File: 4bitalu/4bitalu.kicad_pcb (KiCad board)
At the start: 2 copper layers, 87.6 x 81.3 mm, 34 parts, among them J1 Power, SW1 Opcode, SW2 Input Value, U1 74LS153 - 0, U2 74LS153 - 1, U3 74LS175, U4 74LS283, U5 74LS00 Stage0-1, U6 74LS00 Stage0-2, U7 74LS00 - Stage1

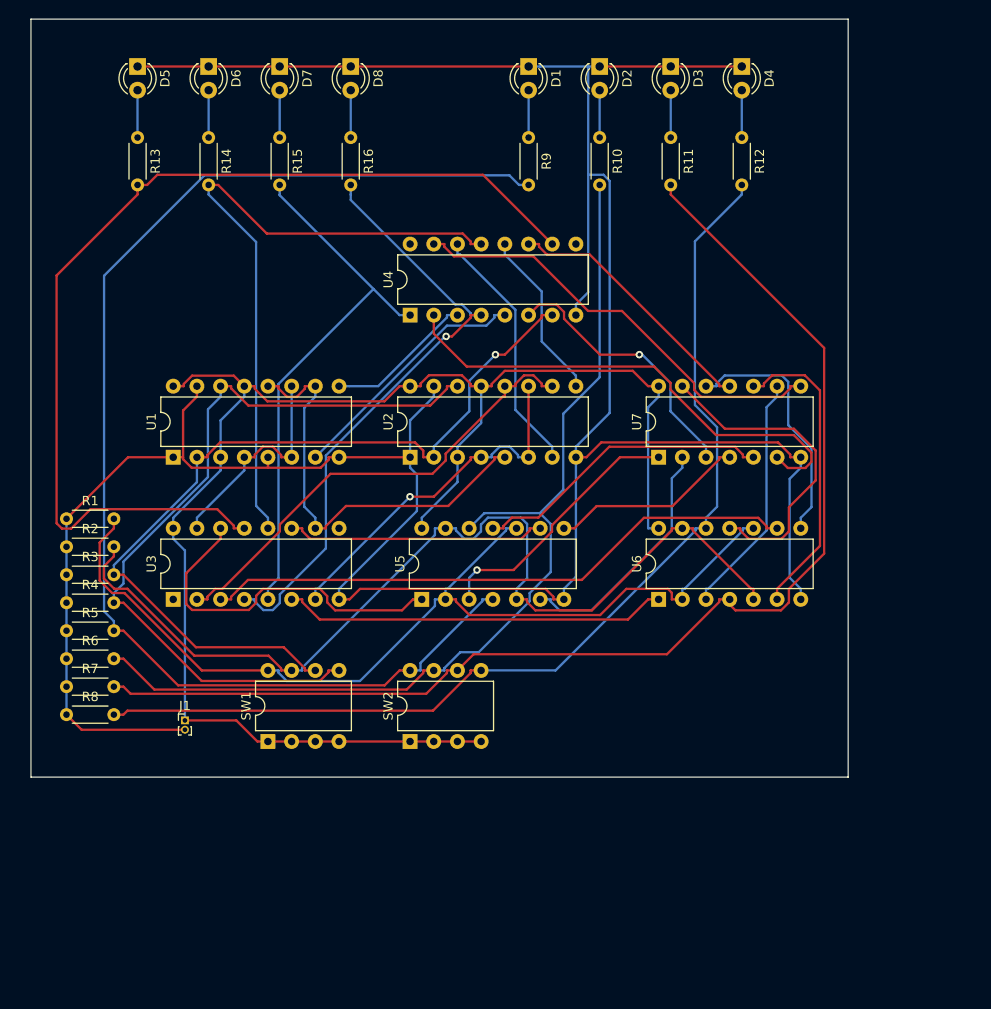
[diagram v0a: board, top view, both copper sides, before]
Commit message: Rev 2 of PCB design
Known issues:

 * Pulldown resistors are too high (should be 1k)
 * Missing capacitors for power inputs on chips
 * Inputs on unused NAND gates are not tied high
 * Clock switch is in unexepected orientation
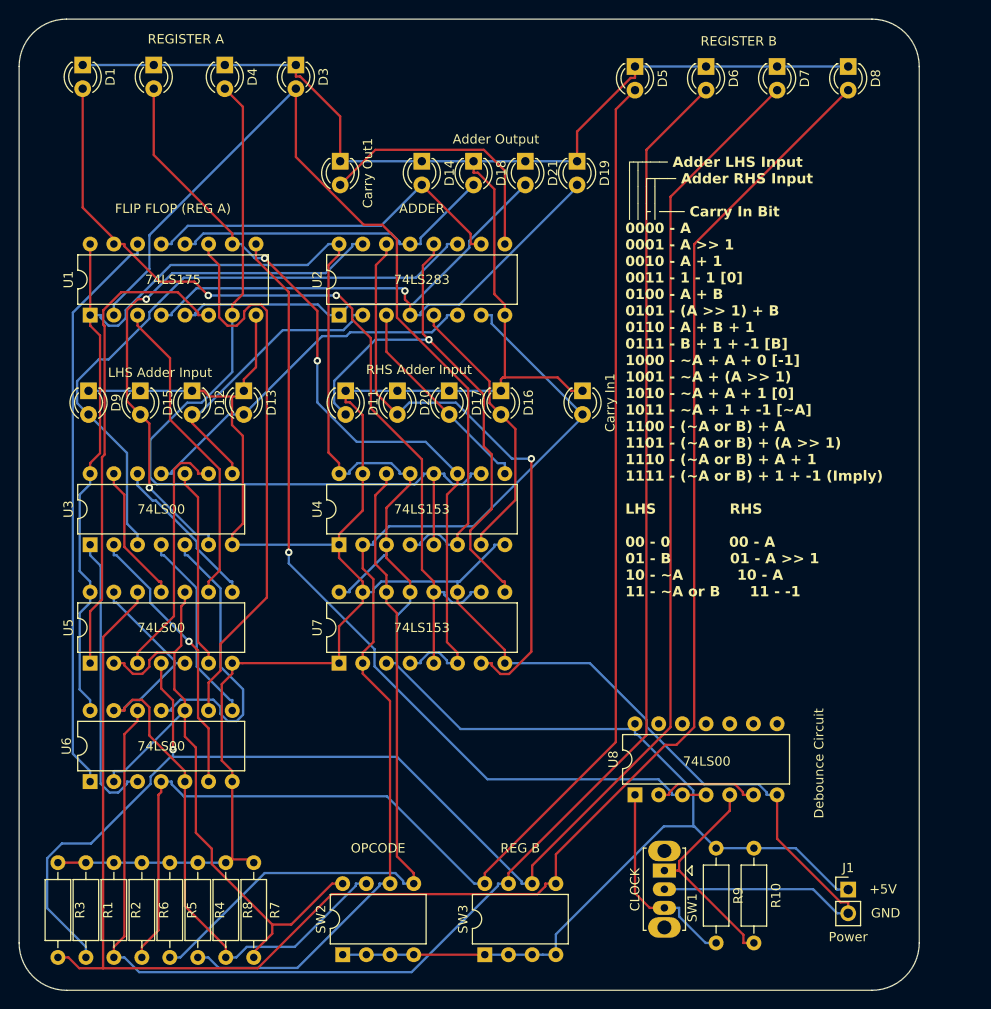
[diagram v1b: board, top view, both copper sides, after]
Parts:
- removed R11, R12, R13, R14, R15, R16: 1.5k, Resistor_THT:R_Axial_DIN0204_L3.6mm_D1.6mm_P5.08mm_Horizontal
- added Carry In1: CarryIn, LED_THT:LED_D3.0mm, F.Cu at (88.4, 93.2)
- added Carry Out1: CarryOut, LED_THT:LED_D3.0mm, F.Cu at (62.4, 68.6)
- added D1: RegBit3, LED_THT:LED_D3.0mm, F.Cu at (34.8, 58.3)
- added D11: RHS3, LED_THT:LED_D3.0mm, F.Cu at (63.0, 93.2)
- added D12: LHS1, LED_THT:LED_D3.0mm, F.Cu at (46.5, 93.2)
- added D13: LHS0, LED_THT:LED_D3.0mm, F.Cu at (52.0, 93.2)
- added D15: LHS2, LED_THT:LED_D3.0mm, F.Cu at (40.9, 93.2)
- added D16: RHS0, LED_THT:LED_D3.0mm, F.Cu at (79.6, 93.2)
- added D17: RHS1, LED_THT:LED_D3.0mm, F.Cu at (74.1, 93.2)
- added D2: RegBit2, LED_THT:LED_D3.0mm, F.Cu at (42.4, 58.3)
- added D20: RHS2, LED_THT:LED_D3.0mm, F.Cu at (68.5, 93.2)
- added D3: RegBit0, LED_THT:LED_D3.0mm, F.Cu at (57.6, 58.3)
- added D4: RegBit1, LED_THT:LED_D3.0mm, F.Cu at (50.0, 58.3)
- added D9: LHS3, LED_THT:LED_D3.0mm, F.Cu at (35.4, 93.2)
- added SW1: SW_SPDT, Button_Switch_THT:SW_Slide_1P2T_CK_OS102011MS2Q, F.Cu at (97.1, 144.6)
- added U8: 74LS00, Package_DIP:DIP-14_W7.62mm, F.Cu at (94.0, 136.5)
- D14: renamed from D5; value RegBit3 -> MidBit3
- D18: renamed from D6; value RegBit2 -> MidBit2
- D19: renamed from D8; value RegBit0 -> MidBit0
- D21: renamed from D7; value RegBit1 -> MidBit1
- J1: footprint Connector_PinHeader_1.00mm:PinHeader_1x02_P1.00mm_Vertical -> Connector_PinHeader_2.54mm:PinHeader_1x02_P2.54mm_Vertical
- R1: renamed from R7; footprint Resistor_THT:R_Axial_DIN0204_L3.6mm_D1.6mm_P5.08mm_Horizontal -> Resistor_THT:R_Axial_DIN0207_L6.3mm_D2.5mm_P10.16mm_Horizontal
- R10, R9: value 1.5k -> 25k; footprint Resistor_THT:R_Axial_DIN0204_L3.6mm_D1.6mm_P5.08mm_Horizontal -> Resistor_THT:R_Axial_DIN0207_L6.3mm_D2.5mm_P10.16mm_Horizontal
- R2: renamed from R6; footprint Resistor_THT:R_Axial_DIN0204_L3.6mm_D1.6mm_P5.08mm_Horizontal -> Resistor_THT:R_Axial_DIN0207_L6.3mm_D2.5mm_P10.16mm_Horizontal
- R3: renamed from R8; footprint Resistor_THT:R_Axial_DIN0204_L3.6mm_D1.6mm_P5.08mm_Horizontal -> Resistor_THT:R_Axial_DIN0207_L6.3mm_D2.5mm_P10.16mm_Horizontal
- R4: renamed from R3; footprint Resistor_THT:R_Axial_DIN0204_L3.6mm_D1.6mm_P5.08mm_Horizontal -> Resistor_THT:R_Axial_DIN0207_L6.3mm_D2.5mm_P10.16mm_Horizontal
- R5: renamed from R4; footprint Resistor_THT:R_Axial_DIN0204_L3.6mm_D1.6mm_P5.08mm_Horizontal -> Resistor_THT:R_Axial_DIN0207_L6.3mm_D2.5mm_P10.16mm_Horizontal
- R6: renamed from R5; footprint Resistor_THT:R_Axial_DIN0204_L3.6mm_D1.6mm_P5.08mm_Horizontal -> Resistor_THT:R_Axial_DIN0207_L6.3mm_D2.5mm_P10.16mm_Horizontal
- R7: renamed from R1; footprint Resistor_THT:R_Axial_DIN0204_L3.6mm_D1.6mm_P5.08mm_Horizontal -> Resistor_THT:R_Axial_DIN0207_L6.3mm_D2.5mm_P10.16mm_Horizontal
- R8: renamed from R2; footprint Resistor_THT:R_Axial_DIN0204_L3.6mm_D1.6mm_P5.08mm_Horizontal -> Resistor_THT:R_Axial_DIN0207_L6.3mm_D2.5mm_P10.16mm_Horizontal
- moved R9 78.8 mm to (102.7, 142.2)
- moved R10 78.0 mm to (106.7, 142.2)
- moved J1 73.4 mm to (116.8, 146.7)
- moved U3 61.7 mm to (35.6, 109.7)
- moved U5 61.3 mm to (35.6, 122.4)
- moved R7 42.0 mm to (53.1, 143.8), turned to -90 degrees
- moved U6 40.6 mm to (35.6, 135.1)
- moved R8 37.9 mm to (50.1, 143.8), turned to -90 degrees
- moved R4 33.9 mm to (47.1, 143.8), turned to -90 degrees
- moved D14 32.1 mm to (71.1, 68.6)
- moved U1 31.8 mm to (35.6, 85.1)
- moved D18 30.2 mm to (76.7, 68.6)
- moved R5 30.0 mm to (44.1, 143.8), turned to -90 degrees
- moved D21 28.2 mm to (82.2, 68.6)
- moved D19 26.3 mm to (87.8, 68.6)
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- renumbered D1 to D5, D2 to D6, D3 to D7, D4 to D8, SW1 to SW2, SW2 to SW3, U3 to U1, U4 to U2, U7 to U3, U1 to U4, U6 to U5, U5 to U6, U2 to U7
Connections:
- D14 pad 2: Net-(D5-A) -> Net-(D14-A)
- D18 pad 2: Net-(D6-A) -> Net-(D18-A)
- D19 pad 2: Net-(D8-A) -> Net-(D19-A)
- D21 pad 2: Net-(D7-A) -> Net-(D21-A)
- D5 pad 2: Net-(D1-A) -> Net-(D5-A)
- D6 pad 2: Net-(D2-A) -> Net-(D6-A)
- D7 pad 2: Net-(D3-A) -> Net-(D7-A)
- D8 pad 2: Net-(D4-A) -> Net-(D8-A)
- R1 pad 2: Net-(R11-Pad2) -> Net-(D7-A)
- R10 pad 1: Net-(D2-A) -> +5V
- R10 pad 2: Net-(R10-Pad2) -> Net-(SW1-A)
- R2 pad 2: Net-(R10-Pad2) -> Net-(D6-A)
- R3 pad 2: Net-(R12-Pad2) -> Net-(D8-A)
- R6 pad 2: Net-(R5-Pad2) -> Net-(D5-A)
- R9 pad 1: Net-(D1-A) -> +5V
- R9 pad 2: Net-(R5-Pad2) -> Net-(SW1-C)
- SW3 pad 5: Net-(R12-Pad2) -> Net-(D8-A)
- SW3 pad 6: Net-(R11-Pad2) -> Net-(D7-A)
- SW3 pad 7: Net-(R10-Pad2) -> Net-(D6-A)
- SW3 pad 8: Net-(R5-Pad2) -> Net-(D5-A)
- U1 pad 1: unconnected-(U3-~{Mr}-Pad1) -> +5V
- U1 pad 10: Net-(U1-I0b) -> Net-(D2-A)
- U1 pad 12: Net-(U3-D2) -> Net-(D18-A)
- U1 pad 13: Net-(U3-D3) -> Net-(D14-A)
- U1 pad 15: Net-(U1-I0a) -> Net-(D1-A)
- U1 pad 2: Net-(U2-I0b) -> Net-(D3-A)
- U1 pad 4: Net-(U3-D0) -> Net-(D19-A)
- U1 pad 5: Net-(U3-D1) -> Net-(D21-A)
- U1 pad 7: Net-(U2-I0a) -> Net-(D4-A)
- U1 pad 9: unconnected-(U3-Cp-Pad9) -> Net-(U1-Cp)
- U2 pad 1: Net-(U3-D1) -> Net-(D21-A)
- U2 pad 10: Net-(U3-D3) -> Net-(D14-A)
- U2 pad 11: Net-(U4-B4) -> Net-(D9-A)
- U2 pad 13: Net-(U3-D2) -> Net-(D18-A)
- U2 pad 15: Net-(U4-B3) -> Net-(D15-A)
- U2 pad 16: unconnected-(U4-VCC-Pad16) -> +5V
- U2 pad 2: Net-(U4-B2) -> Net-(D12-A)
- U2 pad 4: Net-(U3-D0) -> Net-(D19-A)
- U2 pad 6: Net-(U4-B1) -> Net-(D13-A)
- U2 pad 9: unconnected-(U4-C4-Pad9) -> Net-(Carry Out1-A)
- U3 pad 11: Net-(U4-B4) -> Net-(D13-A)
- U3 pad 3: Net-(U4-B1) -> Net-(D9-A)
- U3 pad 6: Net-(U4-B2) -> Net-(D15-A)
- U3 pad 8: Net-(U4-B3) -> Net-(D12-A)
- U4 pad 10: Net-(U1-I0b) -> Net-(D4-A)
- U4 pad 11: Net-(U1-I0a) -> Net-(D2-A)
- U4 pad 12: Net-(U1-I0b) -> Net-(D4-A)
- U4 pad 4: Net-(U1-I0a) -> Net-(D3-A)
- U4 pad 5: GND -> Net-(D4-A)
- U4 pad 6: Net-(U1-I0a) -> Net-(D3-A)
- U5 pad 12: Net-(R12-Pad2) -> Net-(D8-A)
- U5 pad 4: Net-(R11-Pad2) -> Net-(D7-A)
- U6 pad 12: Net-(R10-Pad2) -> Net-(D6-A)
- U6 pad 4: Net-(R5-Pad2) -> Net-(D5-A)
- U7 pad 10: Net-(U2-I0b) -> Net-(D1-A)
- U7 pad 11: Net-(U2-I0a) -> GND
- U7 pad 12: Net-(U2-I0b) -> Net-(D1-A)
- U7 pad 4: Net-(U2-I0a) -> Net-(D2-A)
- U7 pad 5: Net-(U1-I0b) -> Net-(D1-A)
- U7 pad 6: Net-(U2-I0a) -> Net-(D2-A)
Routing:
- net Net-(D8-A): track 5.08 -> 198.4 mm
- net Net-(D7-A): track 5.08 -> 181.6 mm, vias 0 -> 1
- net Net-(D6-A): track 5.08 -> 168.4 mm
- net Net-(D5-A): track 5.08 -> 150.9 mm
- net Net-(R5-Pad2): track 136.4 -> 0.00 mm
- net Net-(R11-Pad2): track 131.8 -> 0.00 mm
- net Net-(R12-Pad2): track 112.4 -> 0.00 mm
- net Net-(U3-D3): track 110.1 -> 0.00 mm
- net Net-(R10-Pad2): track 107.2 -> 0.00 mm
- net +5V: track 164.3 -> 257.1 mm
- net Net-(U1-Cp): track 0.00 -> 91.9 mm, vias 0 -> 1
- net Net-(D3-A): track 5.08 -> 96.9 mm
- net Net-(D1-A): track 5.08 -> 94.8 mm, vias 0 -> 2
- net Net-(D4-A): track 5.08 -> 92.8 mm
- net Net-(D2-A): track 5.08 -> 88.0 mm, vias 0 -> 2
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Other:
- board size 87.6 x 81.3 mm -> 96.5 x 104.1 mm
- board text added: "+5V"
- board text added: "Adder Output"
- board text added: "Debounce Circuit"
- board text added: "GND"
- board text added: "LHS Adder Input"
- board text added: "REGISTER A"
- board text added: "REGISTER B"
- board text added: "RHS Adder Input"
- board text added: "┌┬─── Adder LHS Input ││┌┬── Adder RHS Input ││││ ││├│─── Carry In Bit 0000 - A 0001 - A >> 1 0010 - A + 1 0011 - 1 - 1 [0] 0100 - A + B 0101 - (A >> 1) + B 0110 - A + B + 1 0111 - B + 1 + -1 [B] 1000 - ~A + A + 0 [-1] 1001 - ~A + (A >> 1) 1010 - ~A + A + 1 [0] 1011 - ~A + 1 + -1 [~A] 1100 - (~A or B) + A 1101 - (~A or B) + (A >> 1) 1110 - (~A or B) + A + 1 1111 - (~A or B) + 1 + -1 (Imply) LHS R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"

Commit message: Revision 3 mostly ready
 * Adds caps on power
 * Inverts logic for clock switch
 * Adds optional clock LED
 * Changes pulldown resistors to 1k

Note: this design should also work with 3.3v logic and LEDs
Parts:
- added C1: .1uf, Capacitor_THT:C_Disc_D3.0mm_W1.6mm_P2.50mm, F.Cu at (32.0, 77.5)
- added C2: .1uf, Capacitor_THT:C_Disc_D3.0mm_W1.6mm_P2.50mm, F.Cu at (58.7, 77.5)
- added C3: .1uf, Capacitor_THT:C_Disc_D3.0mm_W1.6mm_P2.50mm, F.Cu at (31.9, 102.1)
- added C4: .1uf, Capacitor_THT:C_Disc_D3.0mm_W1.6mm_P2.50mm, F.Cu at (58.5, 102.0)
- added C5: .1uf, Capacitor_THT:C_Disc_D3.0mm_W1.6mm_P2.50mm, F.Cu at (31.8, 114.7)
- added C6: .1uf, Capacitor_THT:C_Disc_D3.0mm_W1.6mm_P2.50mm, F.Cu at (58.2, 114.8)
- added C7: .1uf, Capacitor_THT:C_Disc_D3.0mm_W1.6mm_P2.50mm, F.Cu at (31.7, 127.5)
- added C8: .1uf, Capacitor_THT:C_Disc_D3.0mm_W1.6mm_P2.50mm, F.Cu at (90.2, 128.9)
- added ClockState1: ClockState, LED_THT:LED_D3.0mm, F.Cu at (104.1, 121.9)
- R1: renamed from R3; value 2k -> 1k
- R2: renamed from R1; value 2k -> 1k
- R3: renamed from R2; value 2k -> 1k
- R4: renamed from R6; value 2k -> 1k
- R5: value 2k -> 1k
- R6: renamed from R4; value 2k -> 1k
- R7: renamed from R8; value 2k -> 1k
- R8: renamed from R7; value 2k -> 1k
- moved R1 9.89 mm to (32.9, 153.6), turned to 90 degrees
- moved R2 9.89 mm to (35.9, 153.6), turned to 90 degrees
- moved R3 9.89 mm to (38.9, 153.6), turned to 90 degrees
- moved R4 9.89 mm to (41.9, 153.6), turned to 90 degrees
- moved R5 9.89 mm to (44.9, 153.6), turned to 90 degrees
- moved R6 9.89 mm to (47.9, 153.6), turned to 90 degrees
- moved R7 9.89 mm to (50.9, 153.6), turned to 90 degrees
- moved R8 9.89 mm to (53.9, 153.6), turned to 90 degrees
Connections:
- U1 pad 9: Net-(U1-Cp) -> Net-(ClockState1-A)
- U8 pad 10: unconnected-(U8-Pad10) -> +5V
- U8 pad 12: unconnected-(U8-Pad12) -> +5V
- U8 pad 13: unconnected-(U8-Pad13) -> +5V
- U8 pad 2: Net-(U8-Pad2) -> Net-(ClockState1-A)
- U8 pad 3: Net-(U1-Cp) -> Net-(U8-Pad3)
- U8 pad 4: Net-(U1-Cp) -> Net-(U8-Pad3)
- U8 pad 6: Net-(U8-Pad2) -> Net-(ClockState1-A)
- U8 pad 9: unconnected-(U8-Pad9) -> +5V
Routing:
- net Net-(ClockState1-A): track 0.00 -> 115.0 mm, vias 0 -> 1
- net GND: track 392.6 -> 498.9 mm
- net Net-(U1-Cp): track 91.9 -> 0.00 mm, vias 1 -> 0
- net +5V: track 257.1 -> 299.1 mm, vias 0 -> 1
- net Net-(D21-A): track 43.8 -> 19.3 mm
- net Net-(D4-A): track 92.8 -> 72.2 mm, vias 0 -> 1
- net Net-(D2-A): track 88.0 -> 108.0 mm, vias 2 -> 1
- net Net-(D20-A): track 64.8 -> 50.1 mm, vias 1 -> 0
- net Net-(R7-Pad2): track 74.0 -> 60.6 mm
- net Net-(U3-Pad5): track 32.0 -> 18.8 mm
- net Net-(D6-A): track 168.4 -> 156.3 mm
- net Net-(D5-A): track 150.9 -> 139.3 mm
- net Net-(U8-Pad2): track 11.4 -> 0.00 mm
- net Net-(D8-A): track 198.4 -> 187.5 mm, vias 0 -> 2
- net Net-(D7-A): track 181.6 -> 171.0 mm, vias 1 -> 2
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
